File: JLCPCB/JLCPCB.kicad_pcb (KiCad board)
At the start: 4 copper layers, 180 x 235 mm, 27 parts

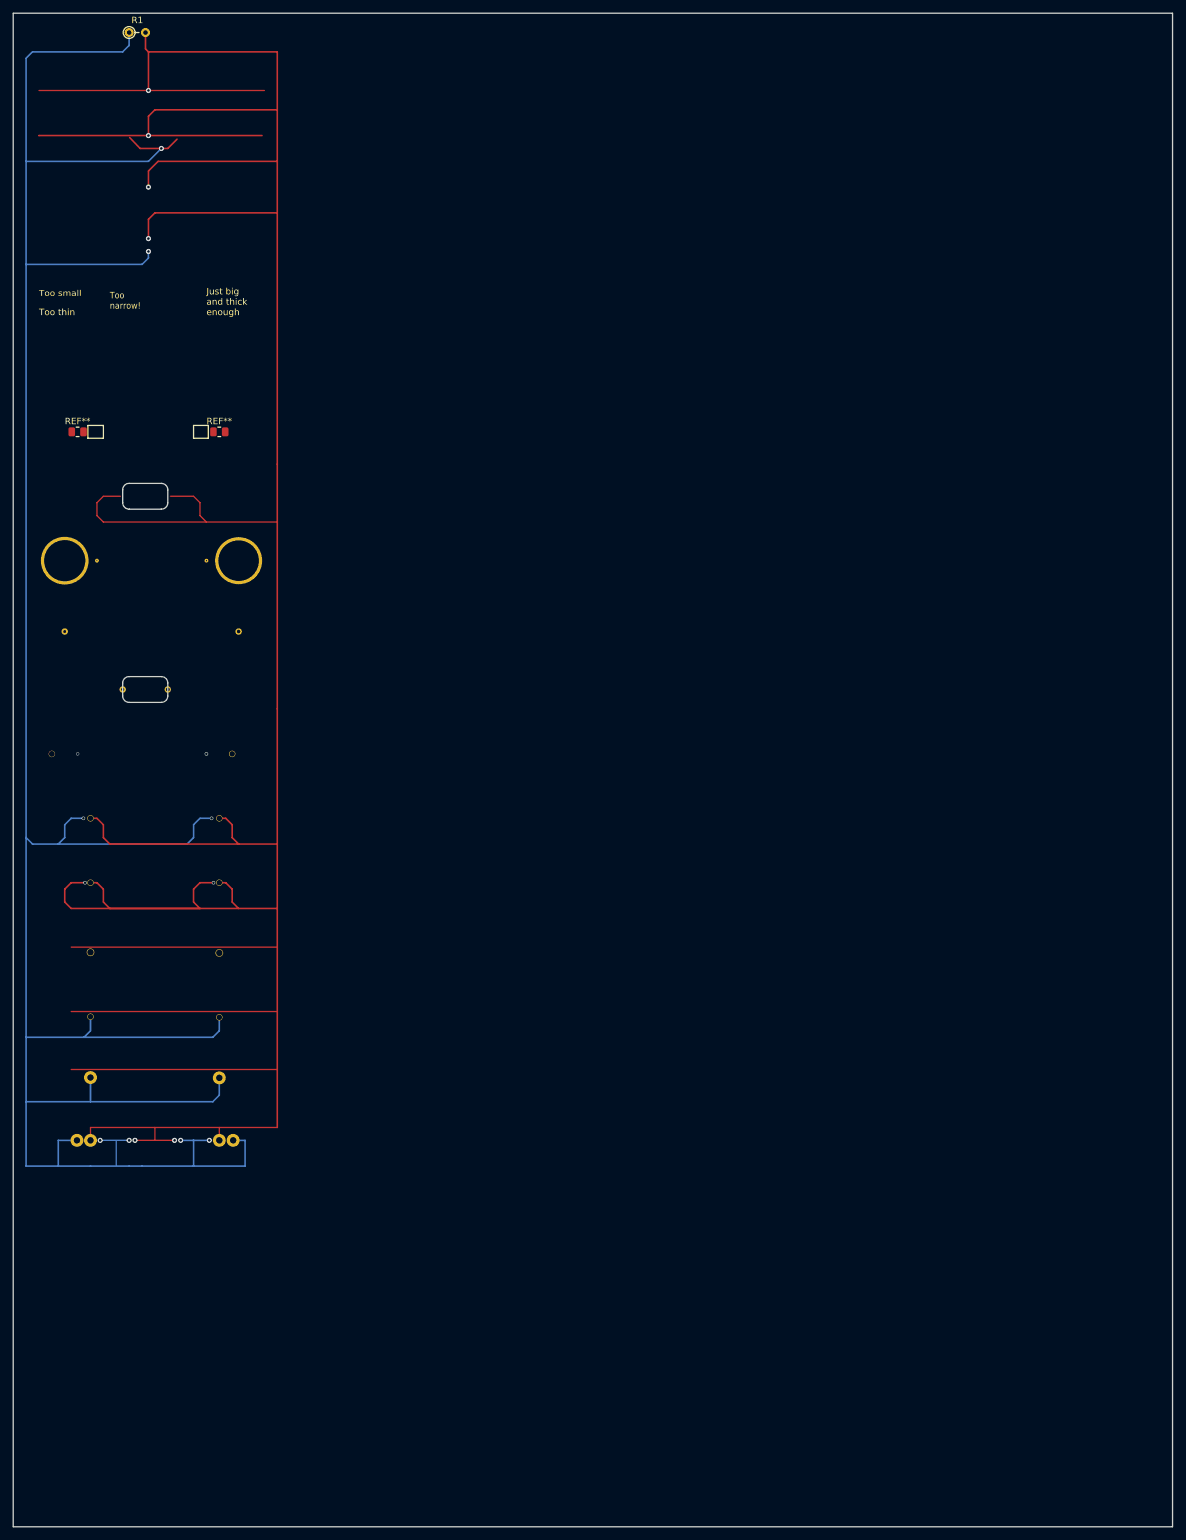
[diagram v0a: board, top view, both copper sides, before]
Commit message: Added DRC rule S-expressions to text box on PCB, next to pass/fail tests of the rule
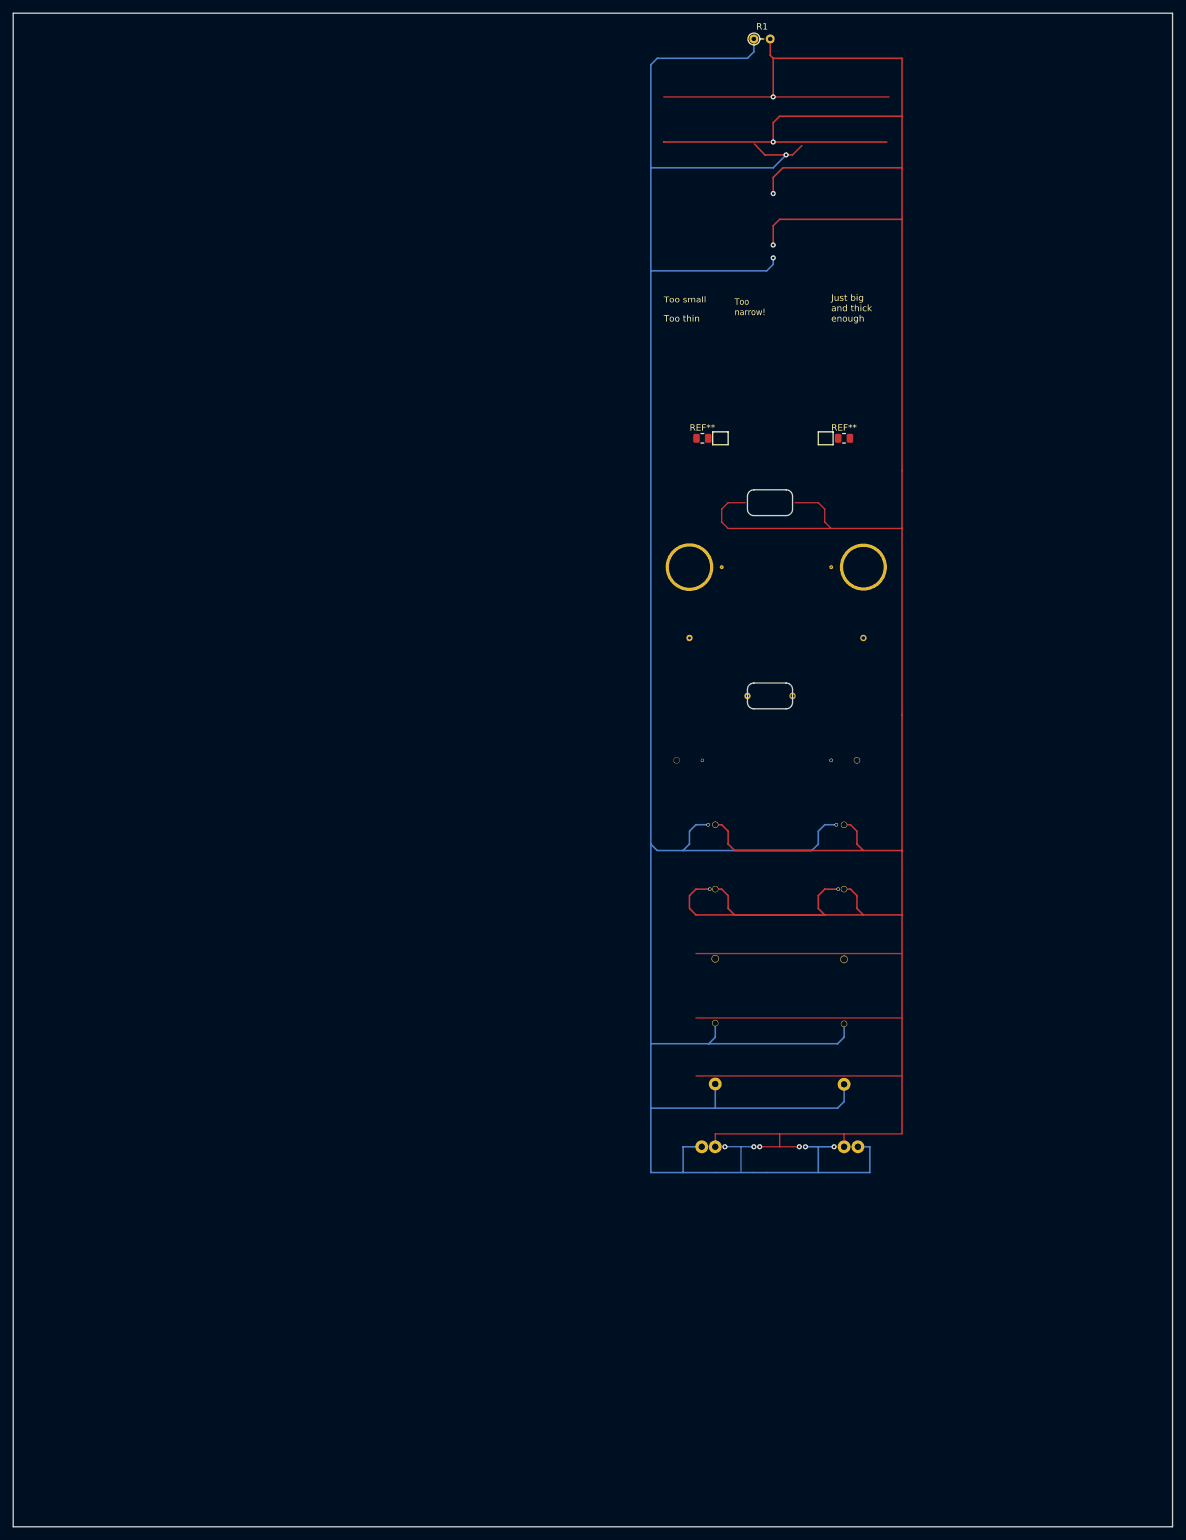
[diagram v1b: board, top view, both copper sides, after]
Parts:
- moved R1 97.0 mm to (129.0, 17.0)
- moved REF** 97.0 mm to (143.0, 79.0)
- moved REF** 97.0 mm to (119.0, 110.0)
- moved REF** 97.0 mm to (121.0, 79.0)
- moved REF** 97.0 mm to (143.0, 159.9)
- moved REF** 97.0 mm to (143.0, 149.0)
- moved REF** 97.0 mm to (143.0, 189.0)
- moved REF** 97.0 mm to (145.2, 189.0)
- moved REF** 97.0 mm to (123.0, 189.0)
- moved REF** 97.0 mm to (123.0, 139.0)
- moved REF** 97.0 mm to (123.0, 169.8)
- moved REF** 97.0 mm to (120.9, 189.0)
- moved REF** 97.0 mm to (141.0, 99.0)
- moved REF** 97.0 mm to (117.0, 129.0)
- moved REF** 97.0 mm to (124.0, 99.0)
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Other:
- outline, holes or cut-outs redrawn

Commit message: Refactor rules.
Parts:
- added ?: , , F.Cu at (121.0, 187.0)
- added ?: , , F.Cu at (145.1, 187.0)
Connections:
- REF** pad 1: GND -> (no net) (x2)
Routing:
- net +5V: track 424.8 -> 429.2 mm
- net GND: track 694.5 -> 696.4 mm, vias 10 -> 8
- net (no net): vias 0 -> 2
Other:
- board text removed: "Too narrow!"

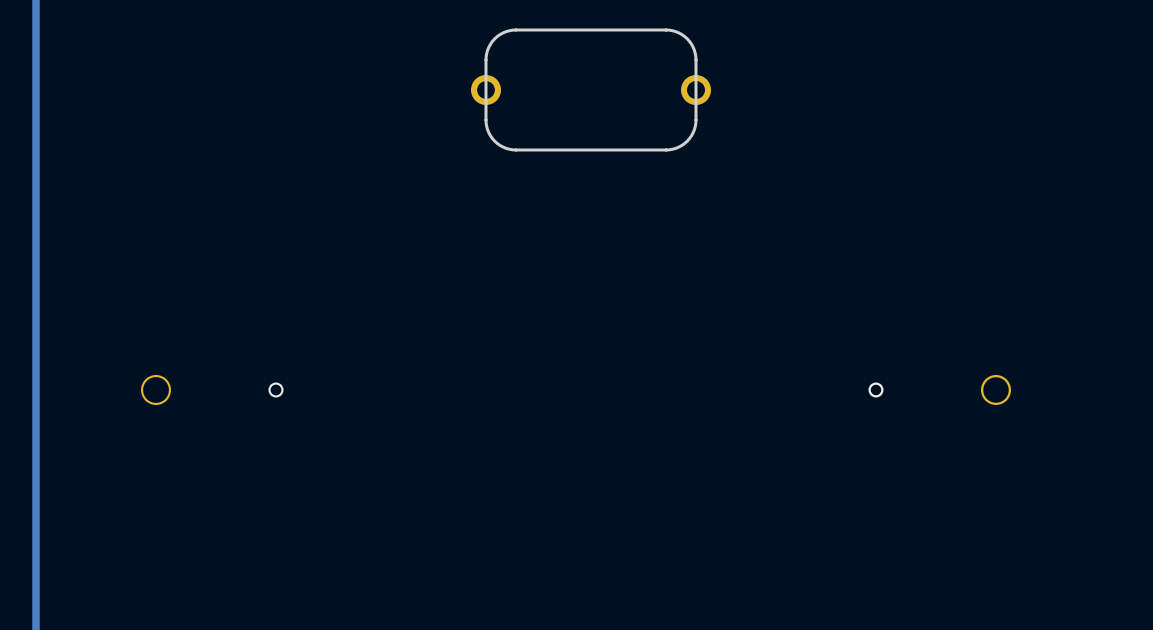
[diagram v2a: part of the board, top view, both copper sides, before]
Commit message: Add “Avoid 4-Wire Kelvin Test” rule.
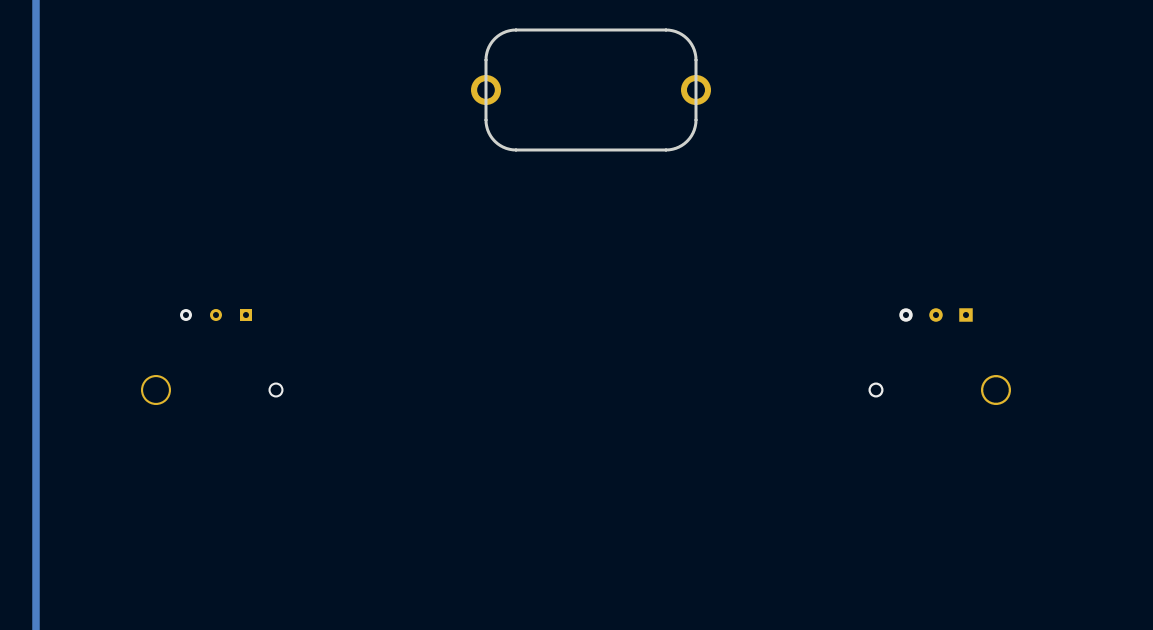
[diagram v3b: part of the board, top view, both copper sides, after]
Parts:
- added ?: , , F.Cu at (143.9, 126.6)
- added ?: , , F.Cu at (143.0, 126.6)
- added ?: , , F.Cu at (119.0, 126.5)
- added ?: , , F.Cu at (120.0, 126.5)
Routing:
- net (no net): vias 2 -> 4
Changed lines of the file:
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@@
       (net 1 "+5V"))
   )
+  (footprint "" (layer "F.Cu")
+    (at 143.95 126.63)
+    (fp_text reference "" (at 0 0) (layer "F.SilkS")
+        (effects (font (size 1.27 1.27) (thickness 0.15)))
+    )
+    (fp_text value "" (at 0 0) (layer "F.SilkS")
+        (effects (font (size 1.27 1.27) (thickness 0.15)))
+    )
+    (pad "" thru_hole rect (at 0.05 -0.13) (size 0.45 0.45) (drill 0.2) (layers "*.Cu" "*.Mask")
+      (pinfunction "VCC") (pintype "passive"))
+  )
   (footprint "MountingHole:MountingHole_2.2mm_M2_DIN965_Pad_TopBottom" (layer "F.Cu")
     (at 128 119)
@@
     )
     (pad "1" thru_hole circle (at 0 0) (size 1 1) (drill 0.59) (property pad_prop_castellated) (layers "*.Cu" "*.Mask"))
+  )
+  (footprint "" (layer "F.Cu")
+    (at 143.01 126.63)
+    (fp_text reference "" (at 0 0) (layer "F.SilkS")
+        (effects (font (size 1.27 1.27) (thickness 0.15)))
+    )
+    (fp_text value "" (at 0 0) (layer "F.SilkS")
+        (effects (font (size 1.27 1.27) (thickness 0.15)))
+    )
+    (pad "" thru_hole circle (at -0.01 -0.13) (size 0.45 0.45) (drill 0.2) (layers "*.Cu" "*.Mask")
+      (pinfunction "VCC") (pintype "passive"))
   )
   (footprint "MountingHole:MountingHole_2.2mm_M2_DIN965_Pad_TopBottom" (layer "F.Cu")
@@
     (pad "1" thru_hole circle (at 0 0) (size 1 1) (drill 0.86) (property pad_prop_castellated) (layers "*.Cu" "*.Mask"))
   )
+  (footprint "" (layer "F.Cu")
+    (at 119 126.5)
+    (fp_text reference "" (at 0 0) (layer "F.SilkS")
+        (effects (font (size 1.27 1.27) (thickness 0.15)))
+    )
+    (fp_text value "" (at 0 0) (layer "F.SilkS")
+        (effects (font (size 1.27 1.27) (thickness 0.15)))
+    )
+    (pad "" thru_hole circle (at 0 0) (size 0.4 0.4) (drill 0.2) (layers "*.Cu" "*.Mask")
+      (pinfunction "VCC") (pintype "passive"))
+  )
   (footprint "MountingHole:MountingHole_2.2mm_M2_DIN965_Pad_TopBottom" (layer "F.Cu")
     (at 124 99)
@@
     )
     (pad "1" thru_hole circle (at 0 0) (size 1 1) (drill 0.85) (property pad_prop_castellated) (layers "*.Cu" "*.Mask"))
+  )
+  (footprint "" (layer "F.Cu")
+    (at 120 126.5)
+    (fp_text reference "" (at 0 0) (layer "F.SilkS")
+        (effects (font (size 1.27 1.27) (thickness 0.15)))
+    )
+    (fp_text value "" (at 0 0) (layer "F.SilkS")
+        (effects (font (size 1.27 1.27) (thickness 0.15)))
+    )
+    (pad "" thru_hole rect (at 0 0) (size 0.4 0.4) (drill 0.2) (layers "*.Cu" "*.Mask")
+      (pinfunction "VCC") (pintype "passive"))
   )
   (footprint "Resistor_THT:R_Axial_DIN0204_L3.6mm_D1.6mm_P2.54mm_Vertical" (layer "F.Cu")
@@
     (stroke (width 0.1) (type solid))  )
   (via (at 141 129) (size 0.5) (drill 0.35) (layers "F.Cu" "B.Cu") (free) (net 0))
+  (via (at 118 126.5) (size 0.4) (drill 0.2) (layers "F.Cu" "B.Cu") (free) (net 0))
   (via (at 121 129) (size 0.5) (drill 0.36) (layers "F.Cu" "B.Cu") (free) (net 0))
+  (via (at 142 126.5) (size 0.45) (drill 0.2) (layers "F.Cu" "B.Cu") (free) (net 0))
   (segment (start 135.29 35) (end 137 33.29) (width 0.2) (layer "F.Cu") (net 1))
   (segment (start 131 35) (end 130.71 35) (width 0.2) (layer "F.Cu") (net 1))
